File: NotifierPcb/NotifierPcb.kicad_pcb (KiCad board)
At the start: 2 copper layers, 20 parts, among them IC1 CD4067BEE4, IC2 ESP32-WROOM-32E__8MB_, J1 RC_433_MHZ_RF, U1 HT75xx-1-SOT89

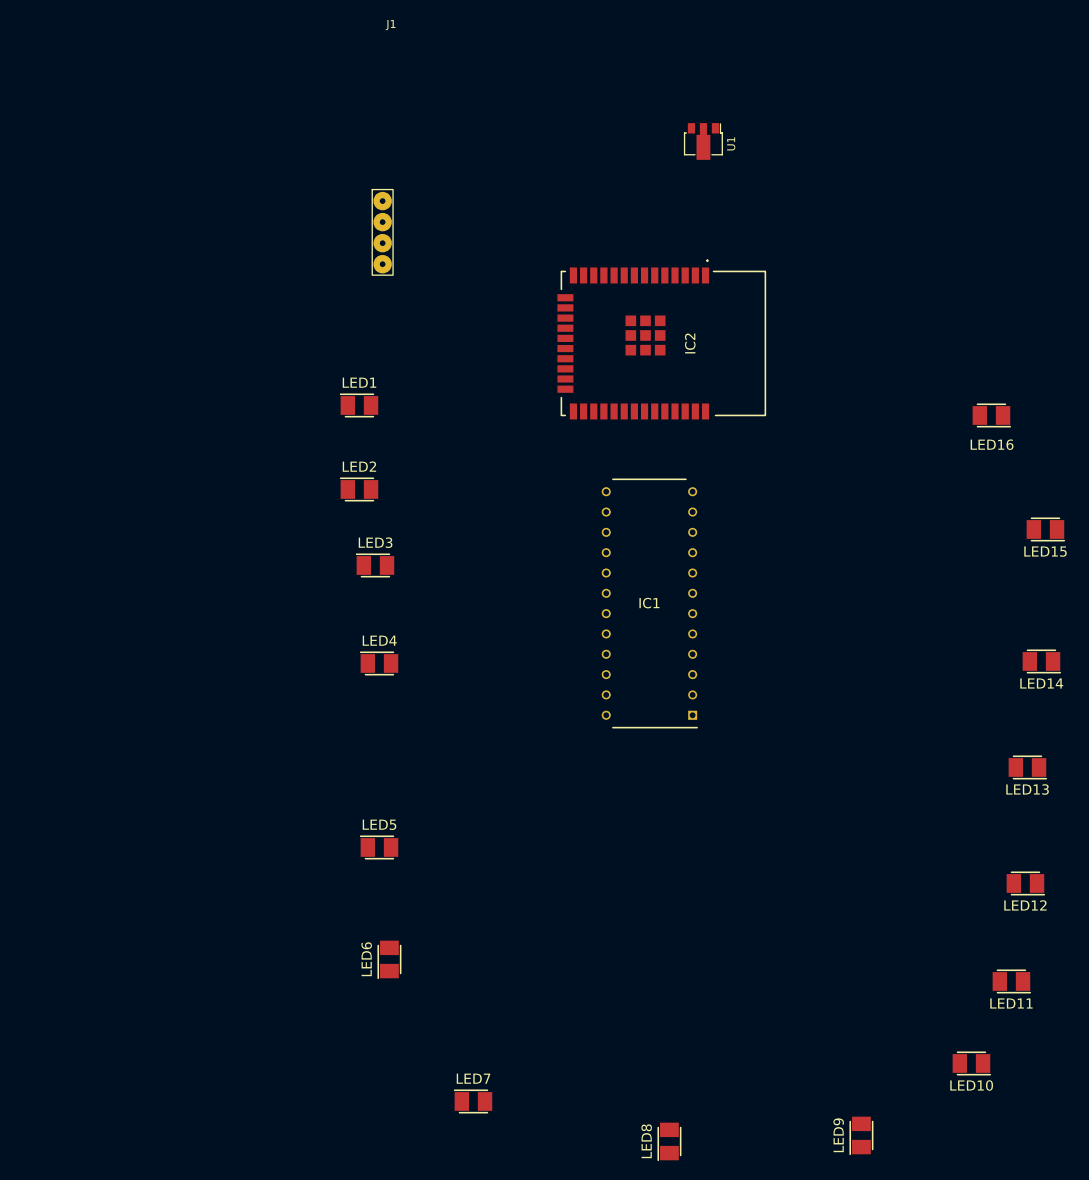
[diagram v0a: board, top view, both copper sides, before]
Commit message: arrange leds in circle, add missing components
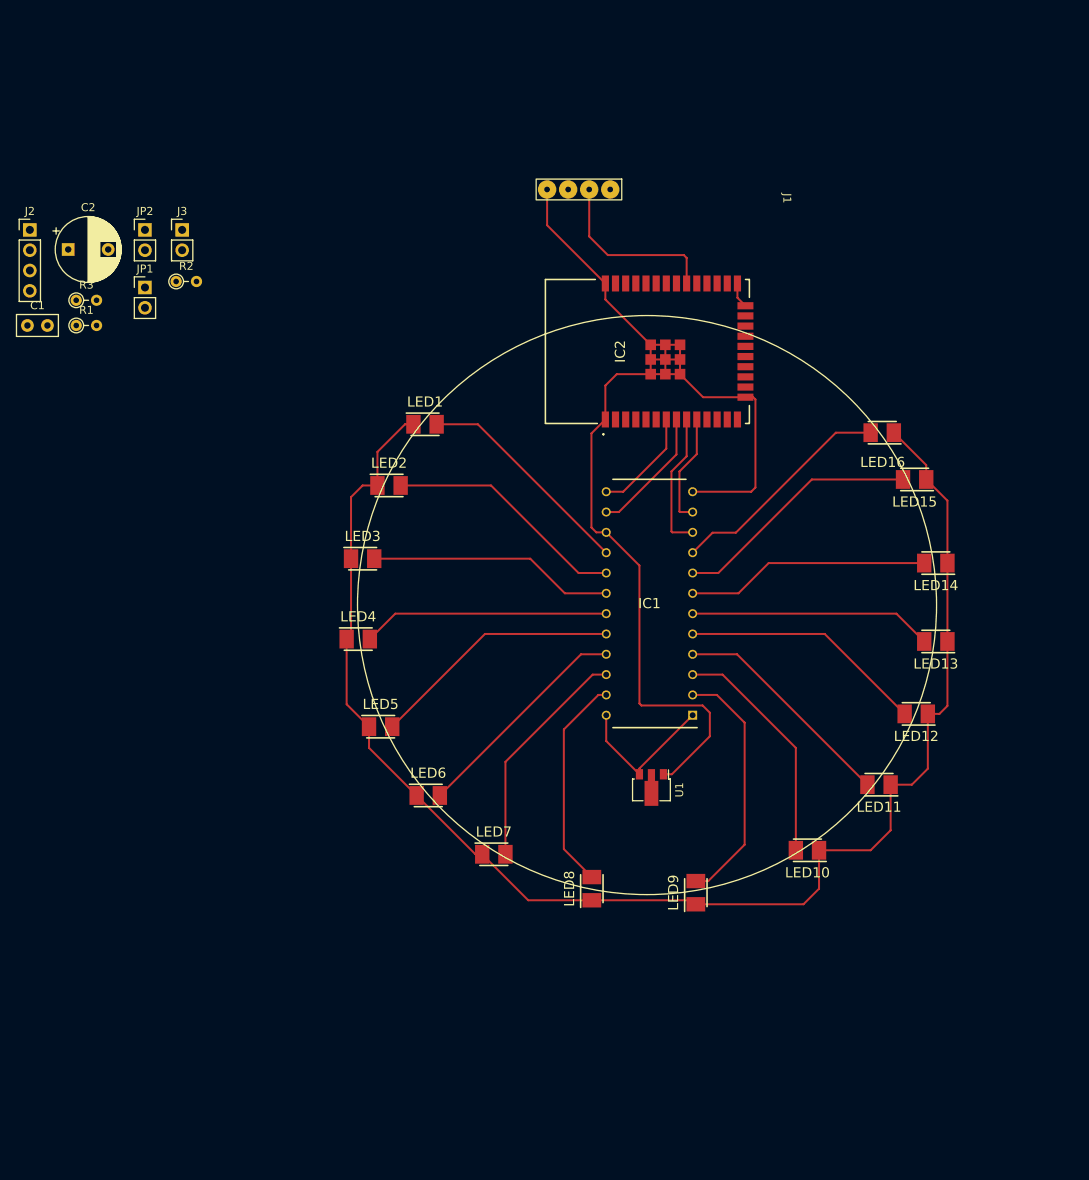
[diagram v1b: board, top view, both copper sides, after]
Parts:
- added C1: 0.1uF, Capacitor_THT:C_Disc_D5.0mm_W2.5mm_P2.50mm, F.Cu at (63.5, 60.8)
- added C2: 4.7uF, Capacitor_THT:CP_Radial_D8.0mm_P5.00mm, F.Cu at (68.6, 51.2)
- added J2: Conn_01x04_Male, Connector_PinHeader_2.54mm:PinHeader_1x04_P2.54mm_Vertical, F.Cu at (63.8, 48.8)
- added J3: Conn_01x02_Male, Connector_PinHeader_2.54mm:PinHeader_1x02_P2.54mm_Vertical, F.Cu at (82.8, 48.8)
- added JP1: Boot_Jumper, Connector_PinHeader_2.54mm:PinHeader_1x02_P2.54mm_Vertical, F.Cu at (78.2, 56.0)
- added JP2: Enable_Jumper, Connector_PinHeader_2.54mm:PinHeader_1x02_P2.54mm_Vertical, F.Cu at (78.2, 48.8)
- added R1: 10kΩ, Resistor_THT:R_Axial_DIN0204_L3.6mm_D1.6mm_P2.54mm_Vertical, F.Cu at (69.6, 60.8)
- added R2: 10kΩ, Resistor_THT:R_Axial_DIN0204_L3.6mm_D1.6mm_P2.54mm_Vertical, F.Cu at (82.1, 55.2)
- added R3: 100Ω, Resistor_THT:R_Axial_DIN0204_L3.6mm_D1.6mm_P2.54mm_Vertical, F.Cu at (69.6, 57.6)
- moved U1 81.0 mm to (141.5, 118.5)
- moved LED9 36.7 mm to (147.1, 131.7)
- moved LED10 33.6 mm to (161.0, 126.3)
- moved LED8 33.1 mm to (134.1, 131.2)
- moved J1 32.3 mm to (141.1, 44.9), turned to -90 degrees
- moved LED7 31.0 mm to (121.8, 126.8)
- moved LED11 29.6 mm to (169.9, 118.2)
- moved LED12 25.2 mm to (174.6, 109.3)
- moved LED6 21.1 mm to (113.6, 119.5), turned to 0 degrees
- moved LED13 19.5 mm to (177.1, 100.2)
- moved LED14 18.0 mm to (177.1, 90.5)
- moved LED15 17.5 mm to (174.4, 80.0)
- moved LED5 15.1 mm to (107.7, 110.9)
- moved LED16 13.8 mm to (170.3, 74.2)
- moved LED1 8.53 mm to (113.2, 73.1)
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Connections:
- IC2 pad 10: BIT3 -> BIT1
- IC2 pad 7: BIT0 -> BIT3
- IC2 pad 8: BIT1 -> BIT2
- IC2 pad 9: BIT2 -> BIT0
- J1 pad 1: (no net) -> +3.3V
- J1 pad 2: (no net) -> RX
- J1 pad 4: (no net) -> GND
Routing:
- net Net-(LED1-Pad1): track 0.00 -> 184.5 mm
- net GND: track 0.00 -> 146.5 mm
- net LED11: track 0.00 -> 31.6 mm
- net LED7: track 0.00 -> 31.2 mm
- net LED1: track 0.00 -> 31.1 mm
- net LED12: track 0.00 -> 30.9 mm
- net LED13: track 0.00 -> 30.8 mm
- net LED4: track 0.00 -> 30.6 mm
- net LED2: track 0.00 -> 30.5 mm
- net LED3: track 0.00 -> 30.4 mm
- net LED14: track 0.00 -> 30.2 mm
- net LED6: track 0.00 -> 29.5 mm
- net LED9: track 0.00 -> 28.7 mm
- net LED5: track 0.00 -> 28.6 mm
- net LED0: track 0.00 -> 28.5 mm
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
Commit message: done pcb beta version
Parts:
- removed JP2: Enable_Jumper, Connector_PinHeader_2.54mm:PinHeader_1x02_P2.54mm_Vertical
- removed R2: 10kΩ, Resistor_THT:R_Axial_DIN0204_L3.6mm_D1.6mm_P2.54mm_Vertical
- added J4: Vcc, Connector_PinHeader_1.00mm:PinHeader_1x01_P1.00mm_Vertical, F.Cu at (164.7, 58.0)
- added J5: Vcc, Connector_PinHeader_1.00mm:PinHeader_1x01_P1.00mm_Vertical, F.Cu at (135.3, 118.5)
- added J6: Vcc, Connector_PinHeader_1.00mm:PinHeader_1x02_P1.00mm_Vertical, F.Cu at (136.9, 77.5)
- J2: value Conn_01x04_Male -> UART_Conn
- J3: value Conn_01x02_Male -> Power_Conn
- moved J2 96.4 mm to (160.1, 53.6), turned to 180 degrees
- moved J3 96.2 mm to (142.8, 124.0), turned to -90 degrees
- moved R1 90.8 mm to (160.4, 58.0), turned to -90 degrees
- moved JP1 83.1 mm to (160.4, 67.8), turned to 180 degrees
- moved C2 43.0 mm to (111.5, 53.7), turned to -90 degrees
- moved R3 42.8 mm to (111.5, 66.1), turned to 90 degrees
- moved C1 40.7 mm to (103.8, 54.8), turned to -90 degrees
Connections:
- IC2 pad 30: RX -> unconnected-(IC2-Pad30)
- IC2 pad 37: unconnected-(IC2-Pad37) -> RX
- J2 pad 1: unconnected-(J2-Pad1) -> GND
- J2 pad 2: unconnected-(J2-Pad2) -> +3.3V
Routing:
- net +3.3V: track 19.2 -> 220.8 mm
- net GND: track 146.5 -> 233.1 mm
- net UART_TX: track 0.00 -> 26.4 mm
- net UART_RX: track 0.00 -> 22.7 mm
- net BOOT: track 3.20 -> 16.0 mm
- net RX: track 22.4 -> 13.6 mm
- net POWER: track 0.00 -> 7.51 mm
- net Net-(LED1-Pad1): track 184.5 -> 191.6 mm

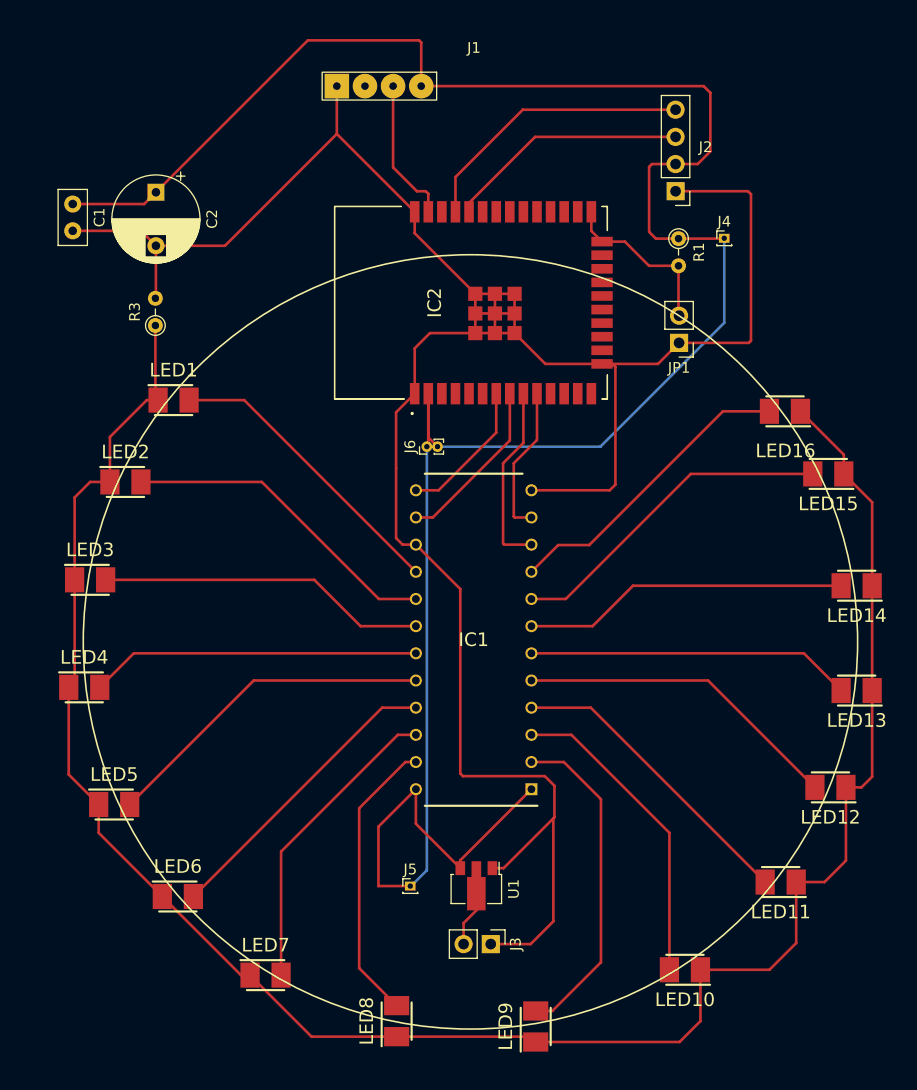
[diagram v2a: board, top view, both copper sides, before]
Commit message: add keepout zone, ground plane£
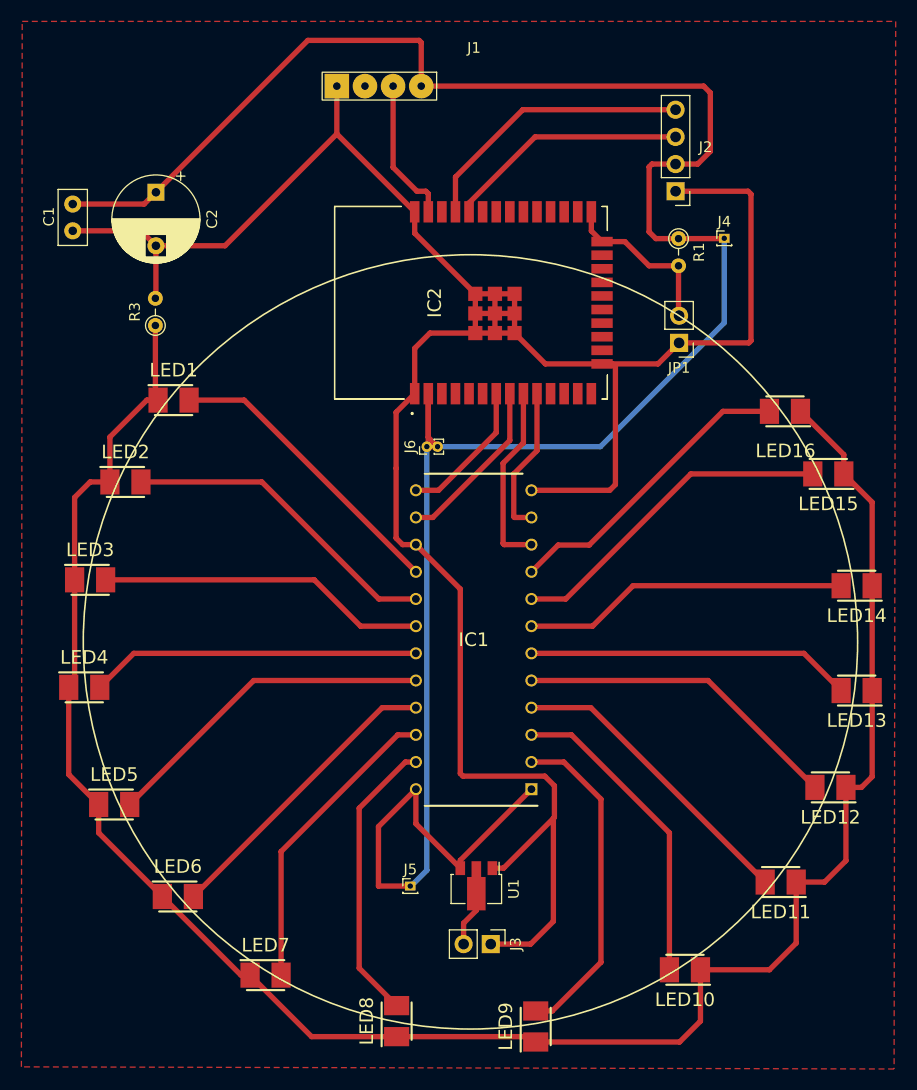
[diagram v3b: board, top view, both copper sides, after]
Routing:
- added copper zone on F.Cu, net GND

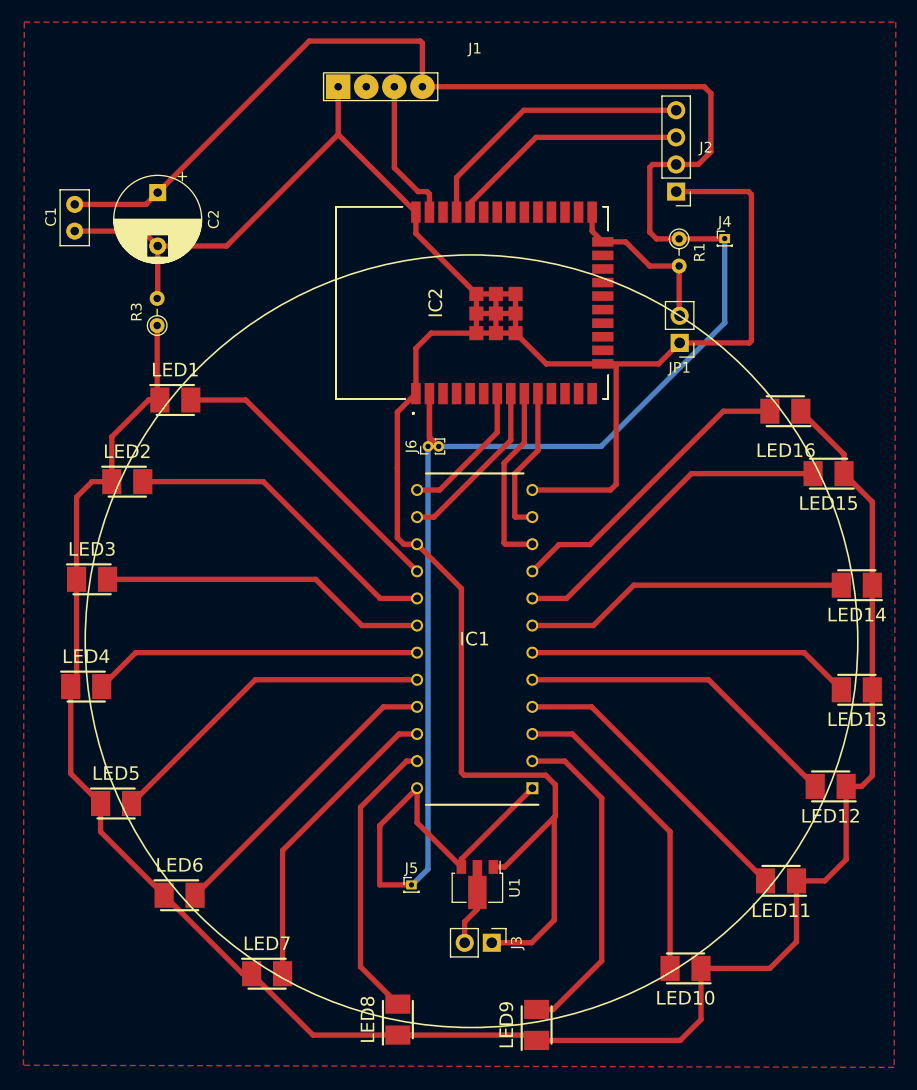
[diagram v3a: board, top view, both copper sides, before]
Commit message: move external margin to Edge.Cuts
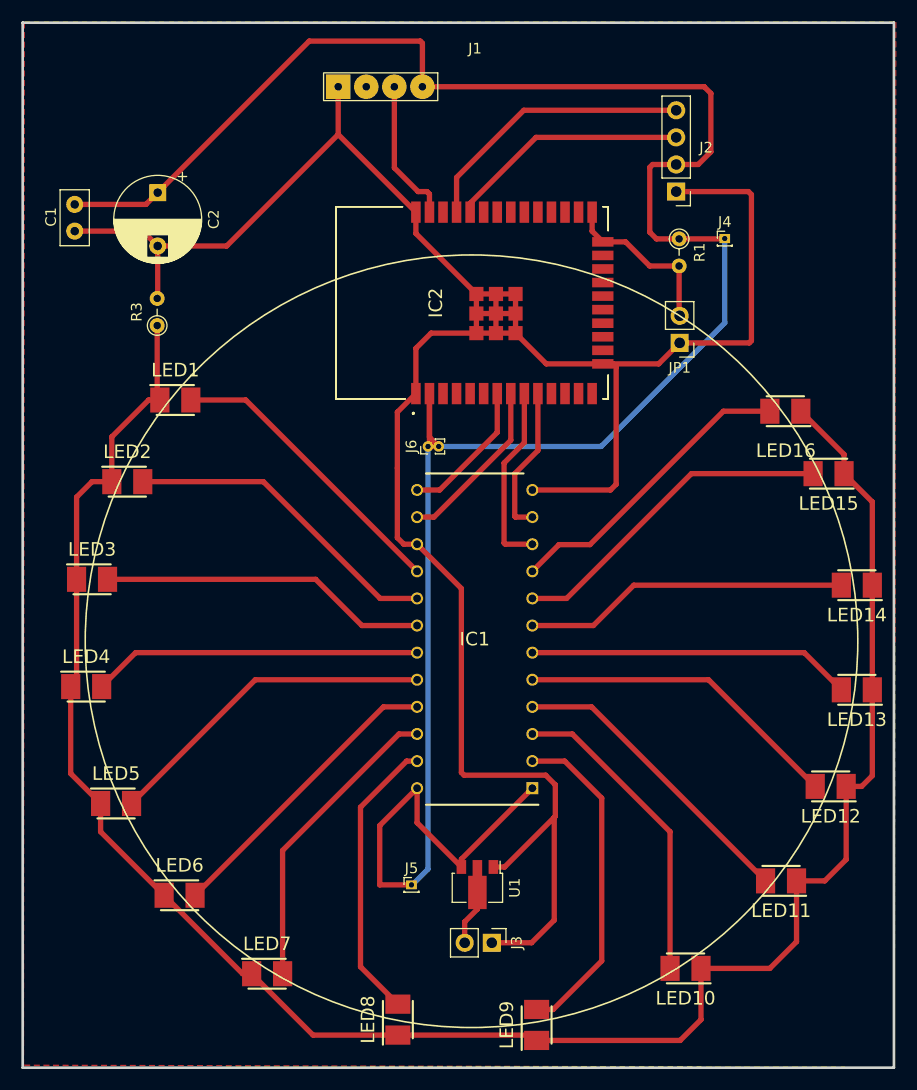
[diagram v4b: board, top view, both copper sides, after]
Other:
- board outline added: 81.6 x 97.9 mm
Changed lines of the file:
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@@
   )
   (gr_circle (center 140.95 95.7) (end 146.25 131.5) (layer "F.SilkS") (width 0.15) (fill none))
-  (gr_rect (start 98.9 37.75) (end 180.525 135.65) (layer "Margin") (width 0.25) (fill none))
+  (gr_rect (start 98.9 37.75) (end 180.525 135.65) (layer "Edge.Cuts") (width 0.25) (fill none))
   (segment (start 135.85 109.47) (end 135.85 112.7) (width 0.5) (layer "F.Cu") (net 1))
   (segment (start 140 116.85) (end 140 116.12) (width 0.5) (layer "F.Cu") (net 1))
